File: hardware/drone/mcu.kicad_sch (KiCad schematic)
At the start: 3 parts, among them SW1 SW_MEC_5E, U1 STM32N645I0

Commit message: cleanup
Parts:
- U1: footprint (none) -> STM32N645I0:BGA178C80P14X14_1200X1200X100
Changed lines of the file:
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@@
 			)
 		)
-		(property "Footprint" ""
+		(property "Footprint" "STM32N645I0:BGA178C80P14X14_1200X1200X100"
 			(at 48.26 66.04 0)
 			(hide yes)

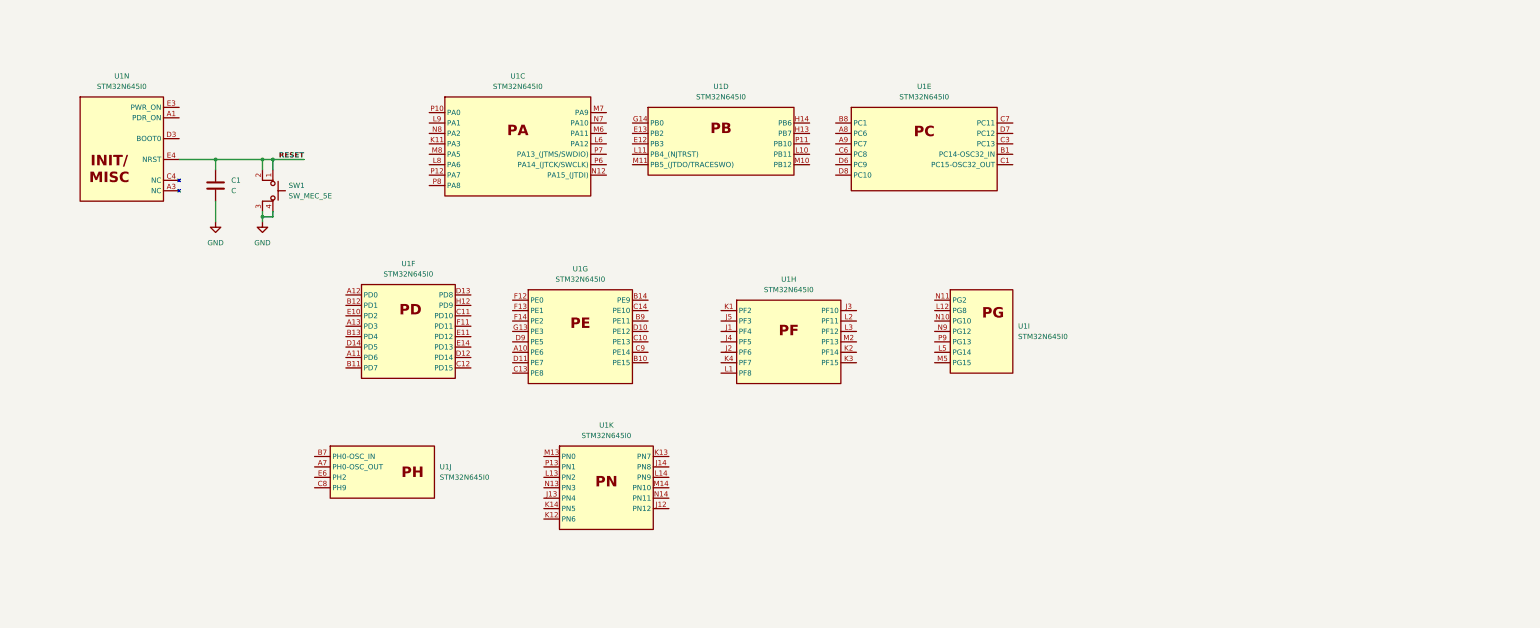
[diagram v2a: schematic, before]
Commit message: More progress on PDN, picked out OSPI chip
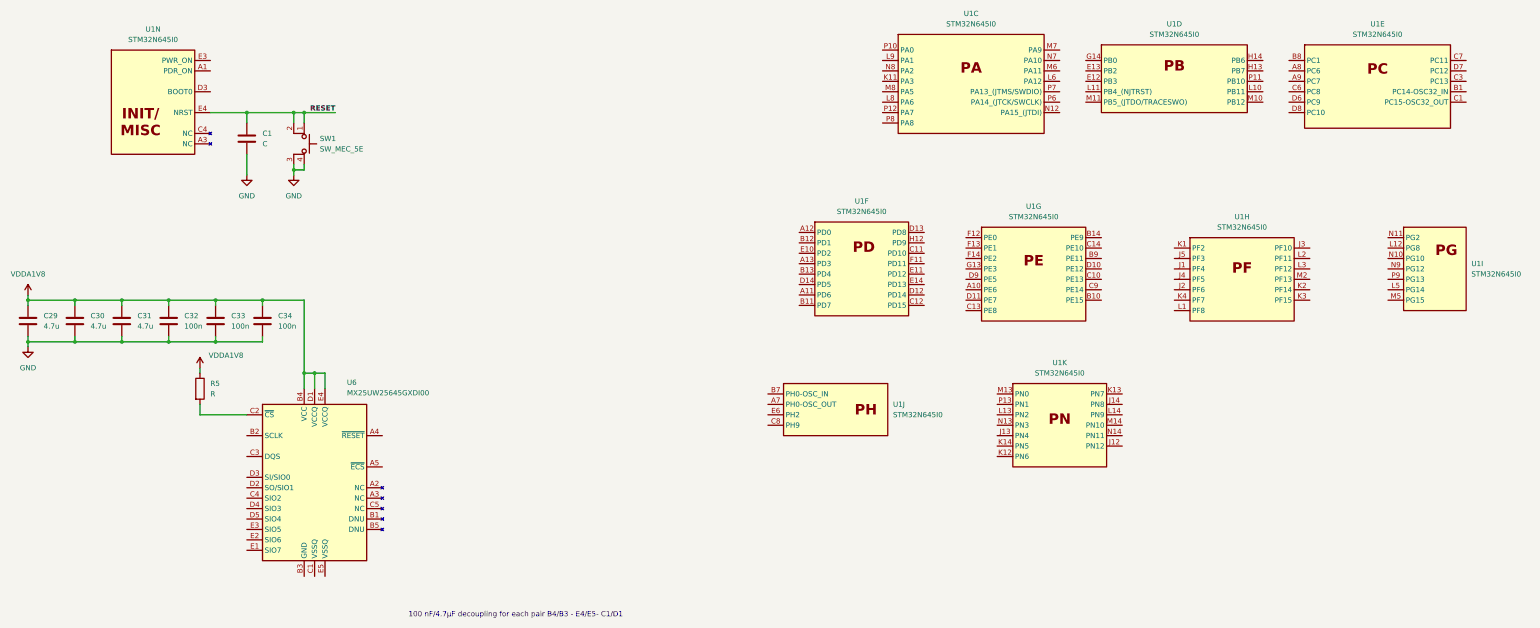
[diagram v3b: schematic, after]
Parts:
- added C29, C30, C31: 4.7u, symbol Device:C
- added C32, C33, C34: 100n, symbol Device:C
- added R5: R, symbol Device:R
- added U6: MX25UW25645GXDI00, BGA24C100P5X5_600X800X120, symbol SoftDrone:MX25UW25645GXDI00
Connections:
- net GND: now also C29.2, C30.2, C31.2, C32.2, C33.2, C34.2
- new net: R5.2, U6.C2 (~{CS})
- new net VDDA1V8: C29.1, C30.1, C31.1, C32.1, C33.1, C34.1, R5.1, U6.B4 (VCC), U6.D1 (VCCQ), U6.E4 (VCCQ)
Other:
- note added: "100 nF/4.7μF decoupling for each pair B4/B3 - E4/E5- C1/D1"
- moved on the sheet: C1, SW1, U1C, U1D, U1E, U1F, U1G, U1H, U1I, U1J, U1K, U1N

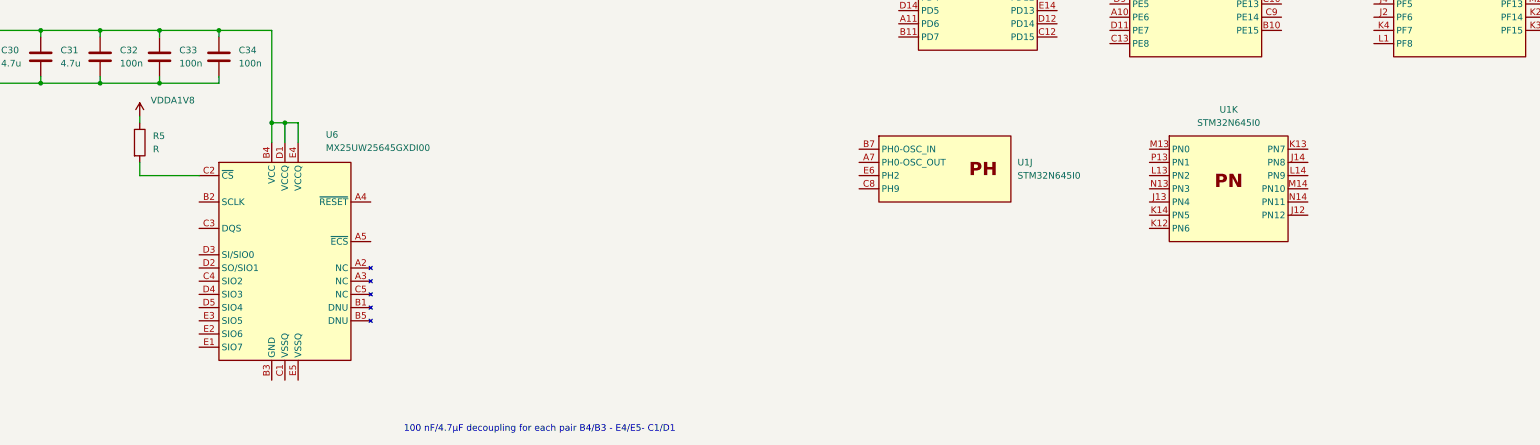
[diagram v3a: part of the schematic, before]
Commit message: Created symbol for CC3350. Almost finished schematic for OSPI
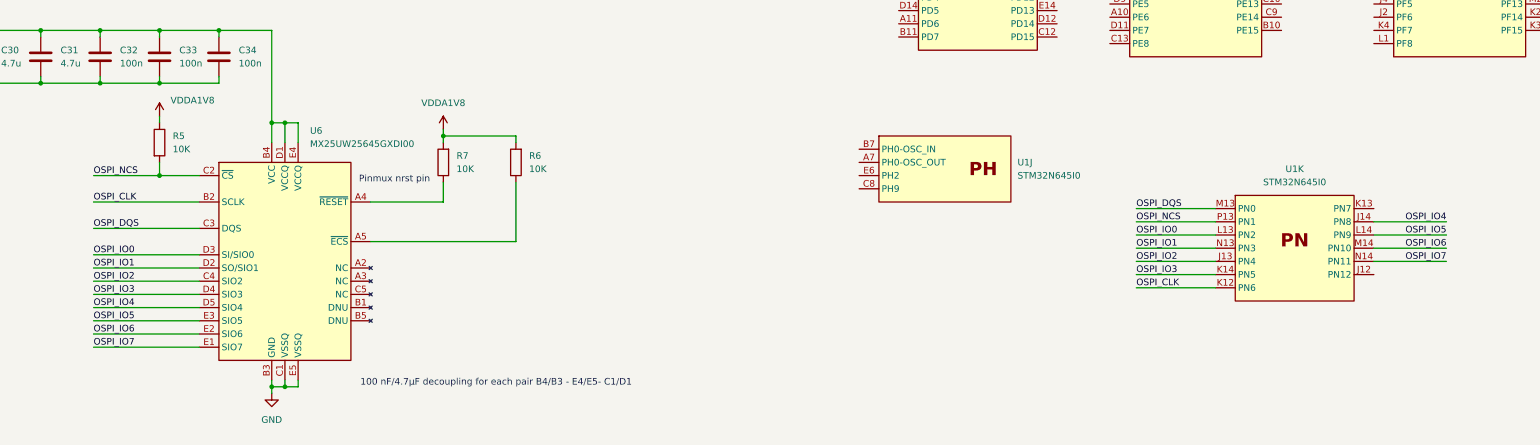
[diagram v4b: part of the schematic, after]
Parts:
- added R6, R7: 10K, symbol Device:R
- R5: value R -> 10K
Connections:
- net GND: now also U6.B3 (GND), U6.C1 (VSSQ), U6.E5 (VSSQ)
- net VDDA1V8: now also R6.2, R7.2
- net OSPI_NCS: now reaches R5.2, U6.C2 (~{CS})
- net OSPI_NCS: now also U1.P13 (PN1)
- net OSPI_IO2: now reaches U1.J13 (PN4)
- net OSPI_IO2: now also U6.C4 (SIO2)
- net OSPI_IO4: now reaches U1.J14 (PN8)
- net OSPI_IO4: now also U6.D5 (SIO4)
- net OSPI_CLK: now reaches U1.K12 (PN6)
- net OSPI_CLK: now also U6.B2 (SCLK)
- net OSPI_IO3: now reaches U1.K14 (PN5)
- net OSPI_IO3: now also U6.D4 (SIO3)
- net OSPI_IO0: now reaches U1.L13 (PN2)
- net OSPI_IO0: now also U6.D3 (SI/SIO0)
- net OSPI_IO5: now reaches U1.L14 (PN9)
- net OSPI_IO5: now also U6.E3 (SIO5)
- net OSPI_DQS: now reaches U1.M13 (PN0)
- net OSPI_DQS: now also U6.C3 (DQS)
- net OSPI_IO6: now reaches U1.M14 (PN10)
- net OSPI_IO6: now also U6.E2 (SIO6)
- net OSPI_IO1: now reaches U1.N13 (PN3)
- net OSPI_IO1: now also U6.D2 (SO/SIO1)
- net OSPI_IO7: now reaches U1.N14 (PN11)
- net OSPI_IO7: now also U6.E1 (SIO7)
- net at U6.A4 (~{RESET}): now also R7.1
- net at U6.A5 (~{ECS}): now also R6.1
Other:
- note added: "Pinmux nrst pin"
- moved on the sheet: R5, U1K

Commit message: more radio work
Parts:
- added C62, C63: C, symbol Device:C
- added unit 13 of U1
- added Y3: Crystal_GND24, symbol Device:Crystal_GND24
- U1: footprint STM32N645I0:BGA178C80P14X14_1200X1200X100 -> (none)
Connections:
- net GND: now also C62.2, C63.2, Y3.2 (G), Y3.4 (G)
- net SX_SPI5_MOSI: now reaches U1.K2 (PF14)
- net SX_SPI5_SCK: now reaches U1.K3 (PF15)
- net SX_SPI5_MISO: now reaches U1.L3 (PF12)
- net SX_SPI5_NSS: now reaches U1.M2 (PF13)
- net CC_SDMMC1_D0: now reaches U1.C6 (PC8)
- net CC_SDMMC1_D3: now reaches U1.C7 (PC11)
- net CC_SDMMC1_D1: now reaches U1.D6 (PC9)
- net CC_SDMMC1_CLK: now reaches U1.D7 (PC12)
- net CC_SDMMC1_D2: now reaches U1.D8 (PC10)
- net at U1.A7 (PH0-OSC_OUT): now also C63.1, Y3.3
- net at U1.B7 (PH0-OSC_IN): now also C62.1, Y3.1
- net CC_SDMMC1_CMD: now reaches U1.E6 (PH2)
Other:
- note added: "OSPI Flash"
- moved on the sheet: C29, C30, C31, C32, C33, C34, R5, R6, R7, U6

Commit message: Fixed SMPS and LDO sequencing issues
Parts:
- U6: footprint BGA24C100P5X5_600X800X120 -> (none)
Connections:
- net PWR_ON: now reaches U1.E3 (PWR_ON)
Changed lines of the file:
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@@
 	(wire
 		(pts
+			(xy 69.85 44.45) (xy 77.47 44.45)
+		)
+		(stroke
+			(width 0)
+			(type default)
+		)
+	)
+	(wire
+		(pts
 			(xy 303.53 91.44) (xy 295.91 91.44)
 		)
@@
 		)
 	)
+	(global_label "PWR_ON"
+		(shape input)
+		(at 77.47 44.45 0)
+		(fields_autoplaced yes)
+		(effects
+			(font
+				(size 1.27 1.27)
+			)
+			(justify left)
+		)
+		(property "Intersheetrefs" "${INTERSHEET_REFS}"
+			(at 88.0752 44.45 0)
+			(hide yes)
+			(show_name no)
+			(do_not_autoplace no)
+			(effects
+				(font
+					(size 1.27 1.27)
+				)
+				(justify left)
+			)
+		)
+	)
 	(global_label "CC_SDMMC1_D1"
 		(shape input)
@@
 			)
 		)
-		(property "Footprint" "BGA24C100P5X5_600X800X120"
+		(property "Footprint" ""
 			(at 119.38 213.36 0)
 			(hide yes)

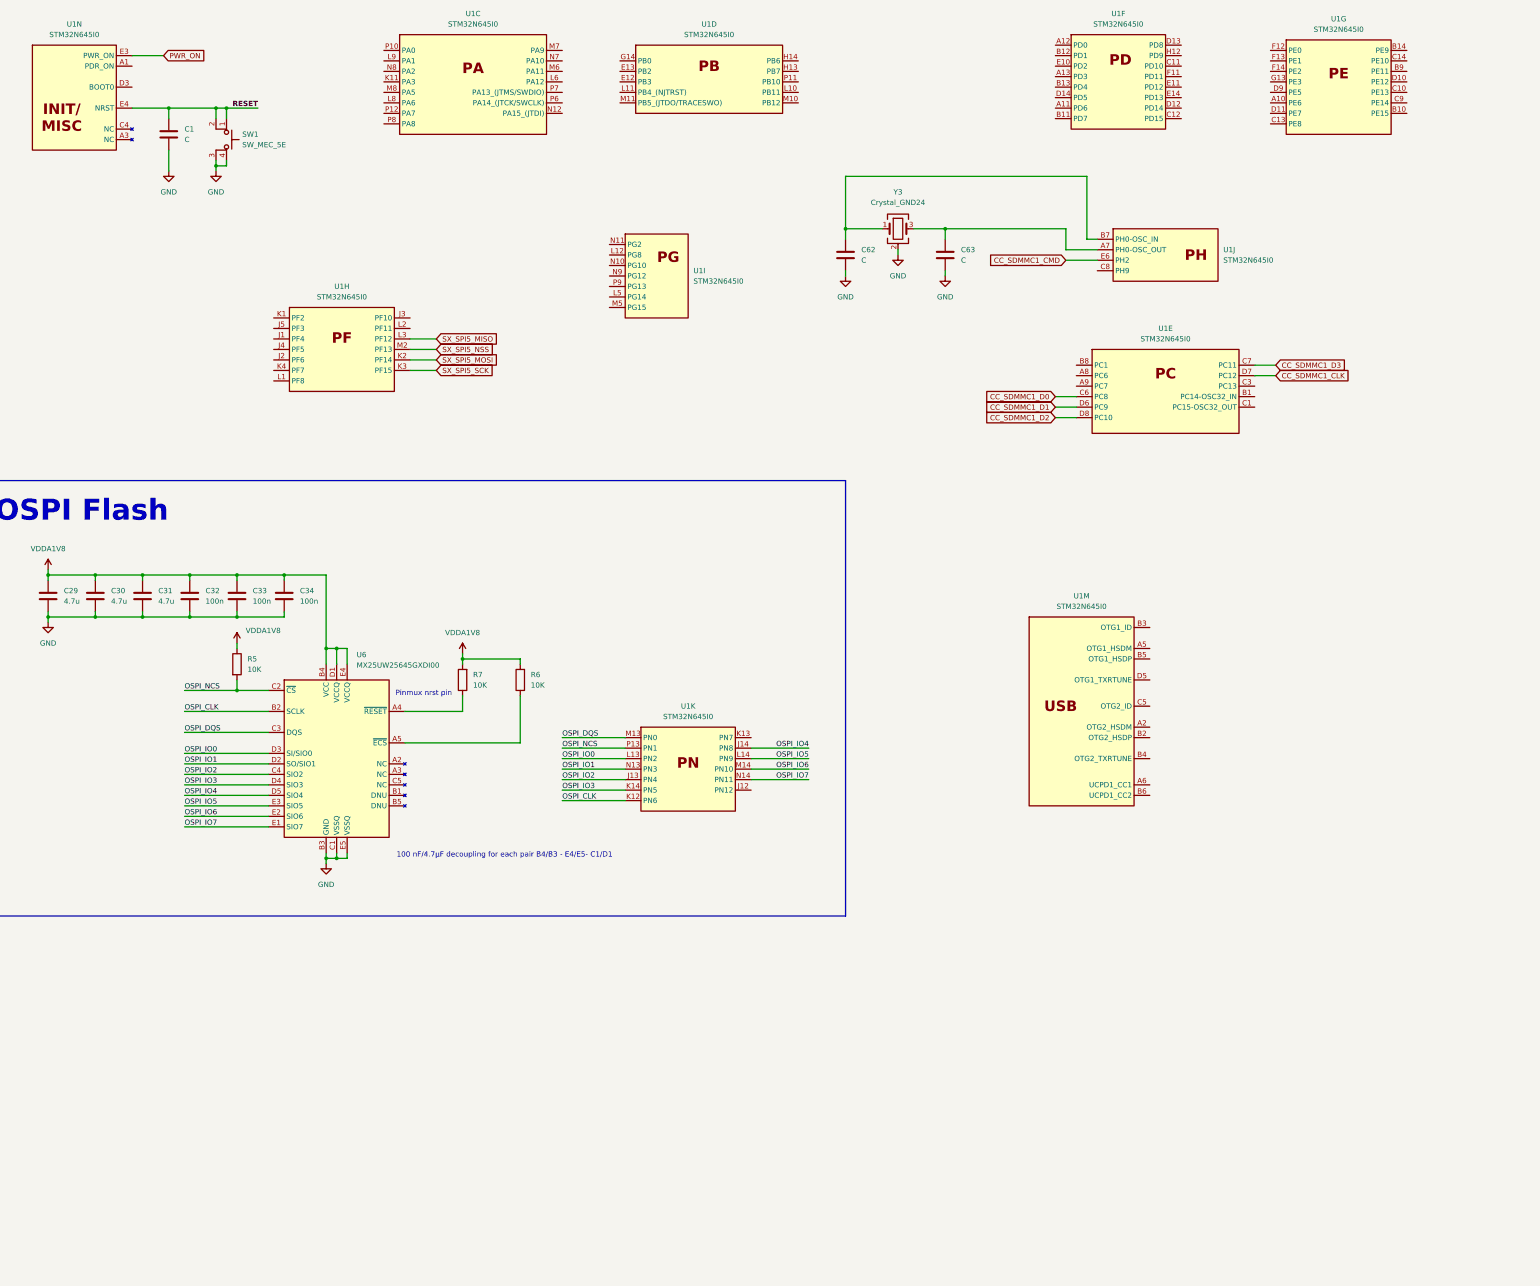
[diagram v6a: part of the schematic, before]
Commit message: Pinmuxxed codec and picked and completed IMU schematic
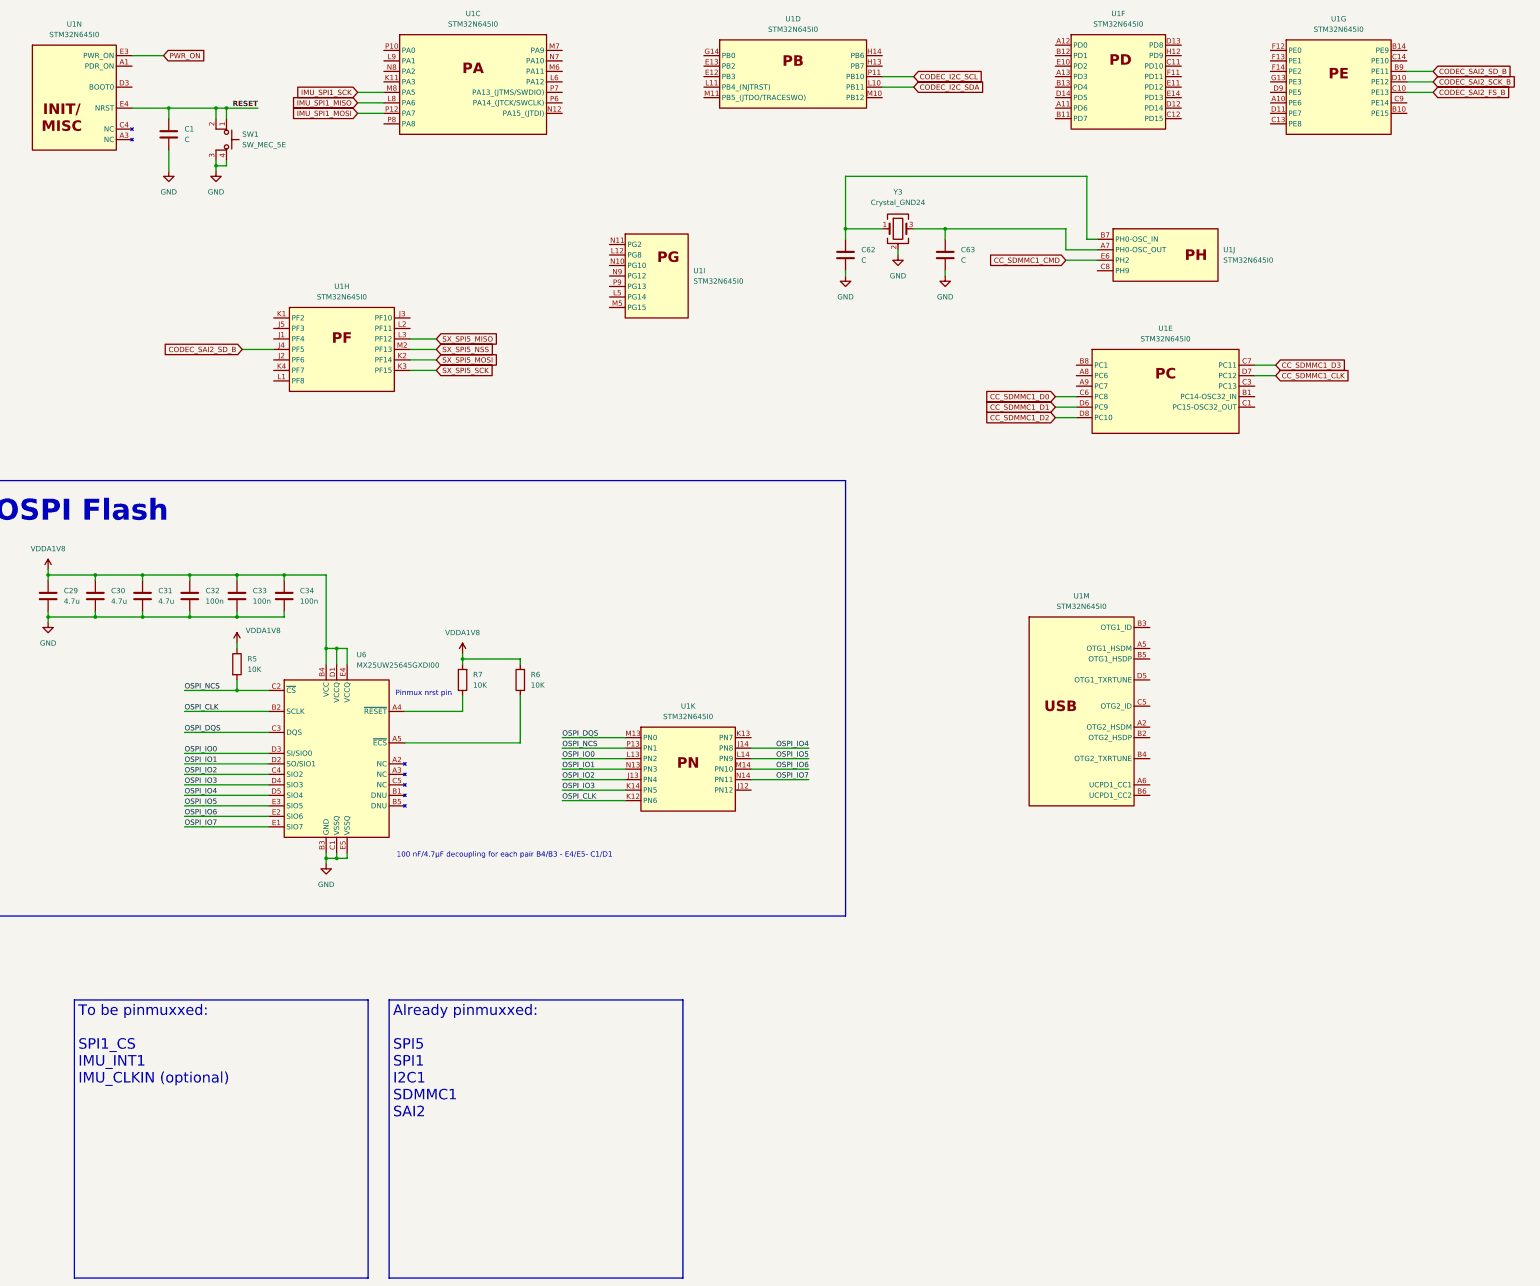
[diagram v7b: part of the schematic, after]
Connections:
- net CODEC_I2C_SDA: now reaches U1.L10 (PB11)
- net CODEC_I2C_SCL: now reaches U1.P11 (PB10)
- net CODEC_SAI2_SD_B: now reaches U1.B9 (PE11)
- net CODEC_SAI2_SD_B: now also U1.J4 (PF5)
- net CODEC_SAI2_FS_B: now reaches U1.C10 (PE13)
- net CODEC_SAI2_SCK_B: now reaches U1.D10 (PE12)
- net IMU_SPI1_MISO: now reaches U1.L8 (PA6)
- net IMU_SPI1_SCK: now reaches U1.M8 (PA5)
- net IMU_SPI1_MOSI: now reaches U1.P12 (PA7)
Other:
- moved on the sheet: U1D

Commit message: Finished GNSS, did more pinmuxxing
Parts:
- added R13, R14: 10k, symbol Device:R
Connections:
- net GNSS_UART4_RX_1V8: now reaches U1.A12 (PD0)
- net GNSS_UART4_TX_1V8: now reaches U1.B12 (PD1)
- net CODEC_I2C_SCL renamed CODEC_I2C2_SCL
- net CODEC_I2C2_SCL: now also R14.2
- net CODEC_I2C_SDA renamed CODEC_I2C2_SDA
- net CODEC_I2C2_SDA: now also R13.2
- new net VDD1V8: R13.1, R14.1
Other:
- moved on the sheet: U1F, U1G
